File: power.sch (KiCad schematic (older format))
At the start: 8 parts

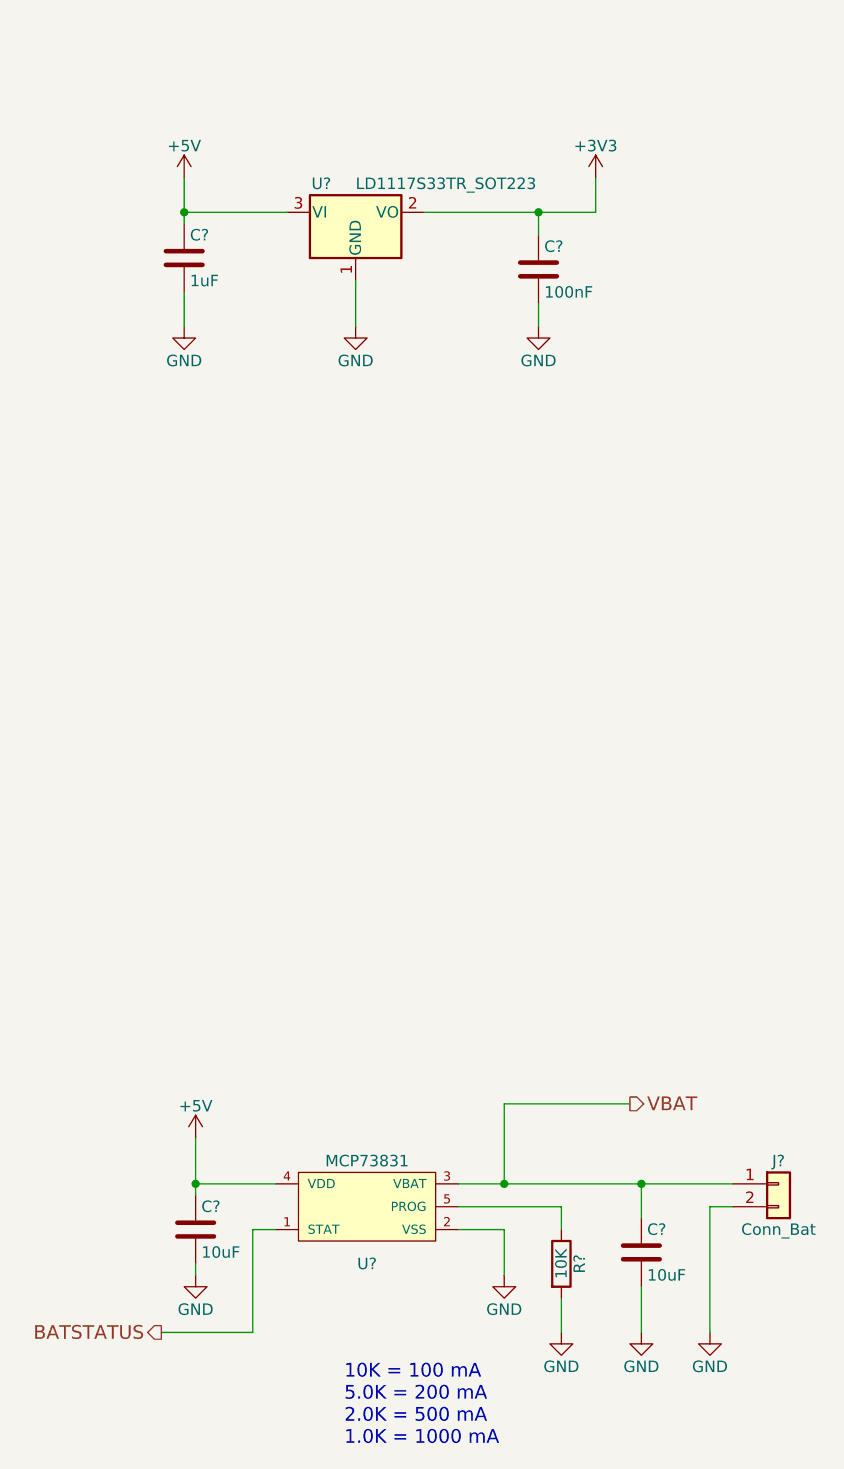
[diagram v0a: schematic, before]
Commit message: Improve battery as power source
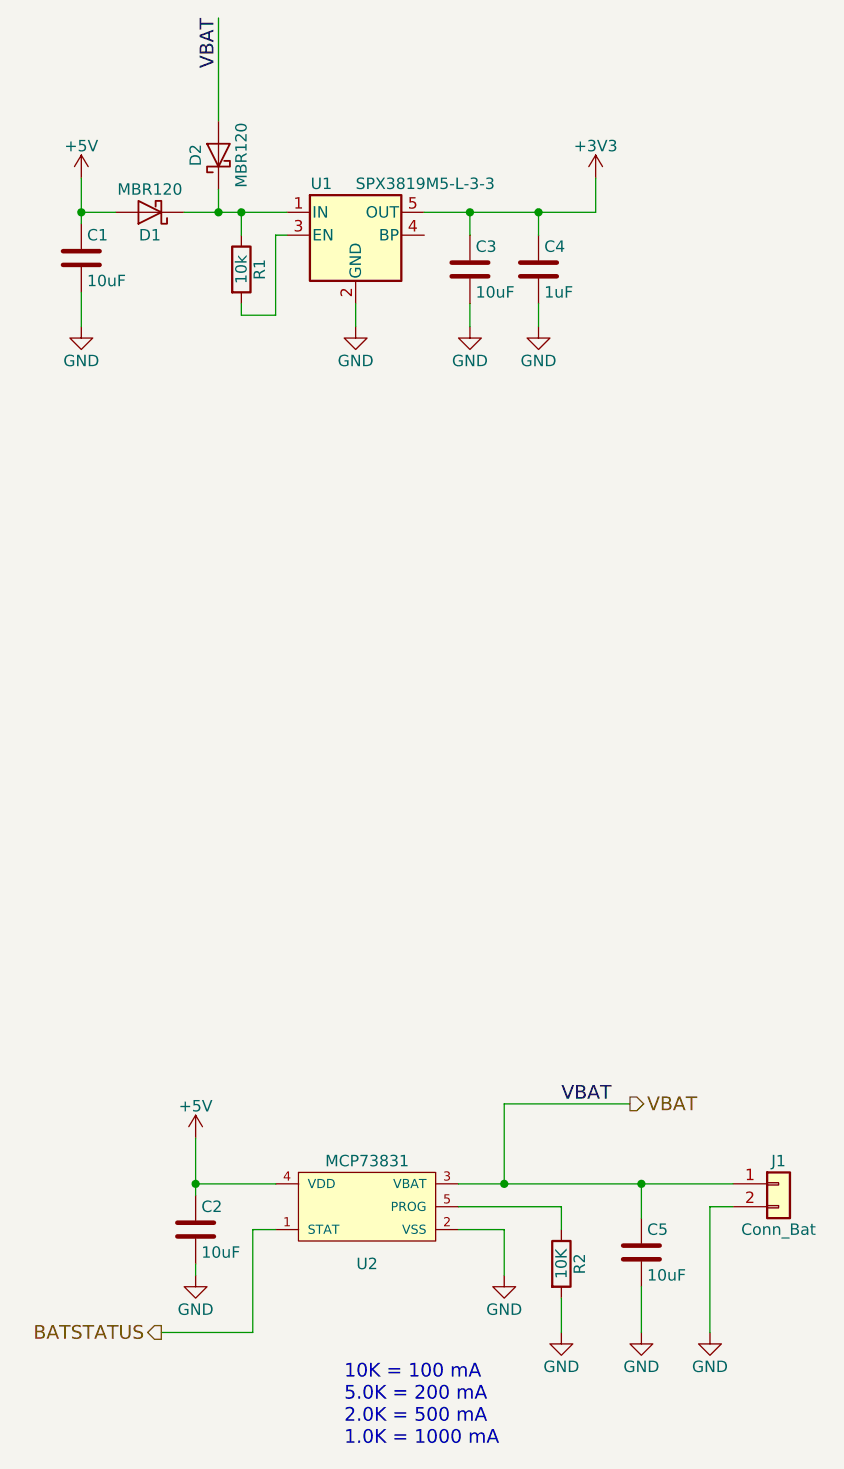
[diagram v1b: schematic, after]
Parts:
- removed U?: LD1117S33TR_SOT223, TO_SOT_Packages_SMD:SOT-223-3Lead_TabPin2, symbol LD1117S33TR_SOT223
- added C4: 1uF, symbol C
- added D1, D2: MBR120, symbol D_Schottky
- added R1: 10k, symbol R
- added U1: SPX3819M5-L-3-3, TO_SOT_Packages_SMD:SOT-23-5, symbol SPX3819M5-L-3-3
- C1: renamed from C?; value 1uF -> 10uF
- C3: renamed from C?; value 100nF -> 10uF
- gave numbers to parts that had none: 5
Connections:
- net +3V3: now also C4.1, U1.5 (OUT)
- net +5V: now also D1.2 (A)
- net GND: now also C4.2, U1.2 (GND)
- net VBAT: now also D2.2 (A)
- new net: D1.1 (K), D2.1 (K), R1.1, U1.1 (IN)
- new net: R1.2, U1.3 (EN)
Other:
- moved on the sheet: C1, C3
